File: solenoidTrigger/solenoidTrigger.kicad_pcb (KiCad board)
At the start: 2 copper layers, 88.9 x 88.9 mm, 44 parts, among them J1 Conn_01x09_Female, J8 CONN_02X03, P1 OSTTC03, P2 OSTTC02, P4 OSTTC03, Q1 NMOS_CDS16, Q2 NMOS_CDS16, Q4 NMOS_CDS16, Q5 NMOS_CDS16, U1 L78M05CDT-TR, U2 ATmega328P-AU, Y2 Crystal_SMD

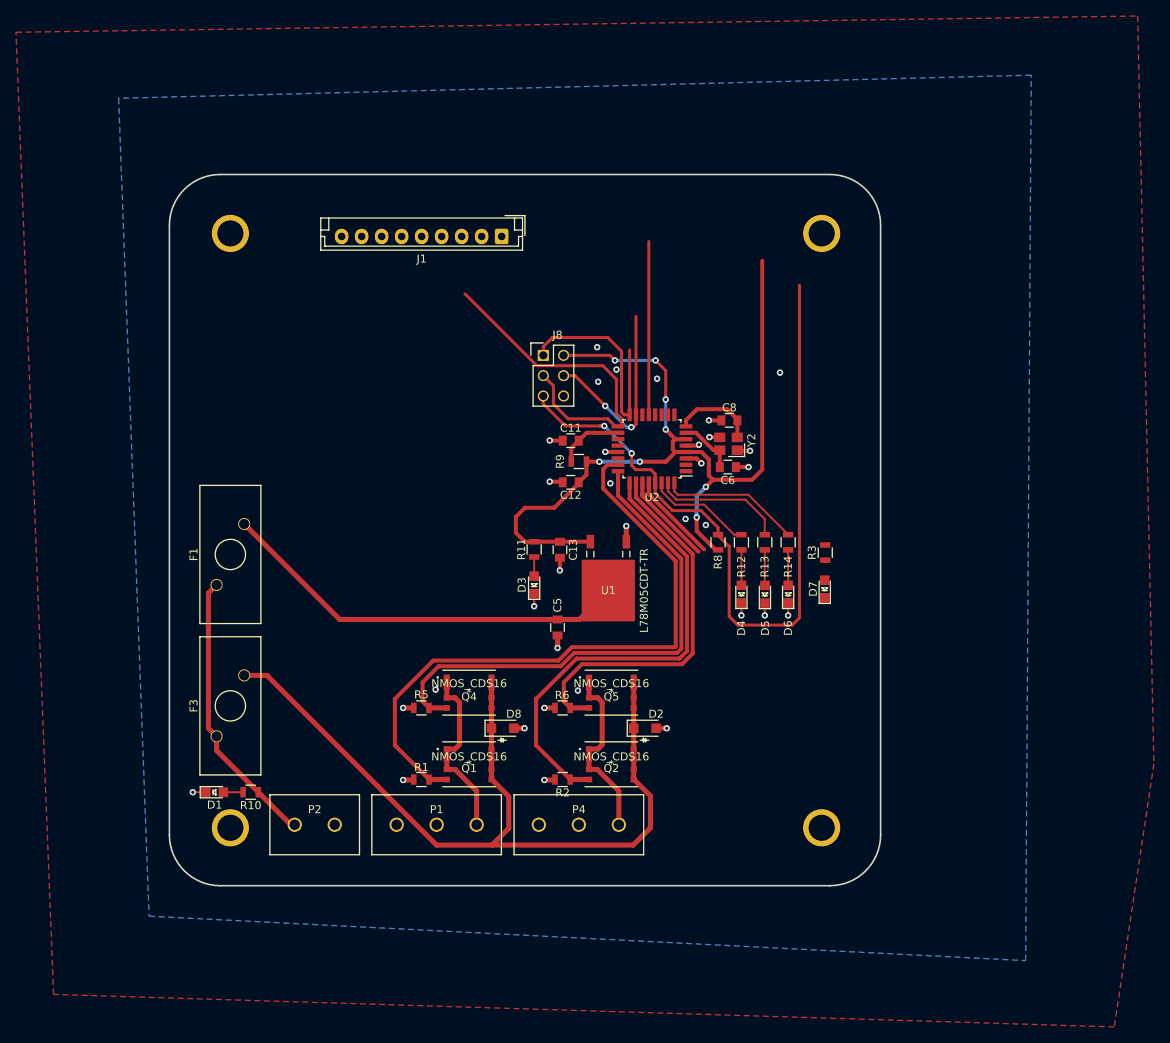
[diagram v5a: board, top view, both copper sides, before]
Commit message: moved components away from mounting holes
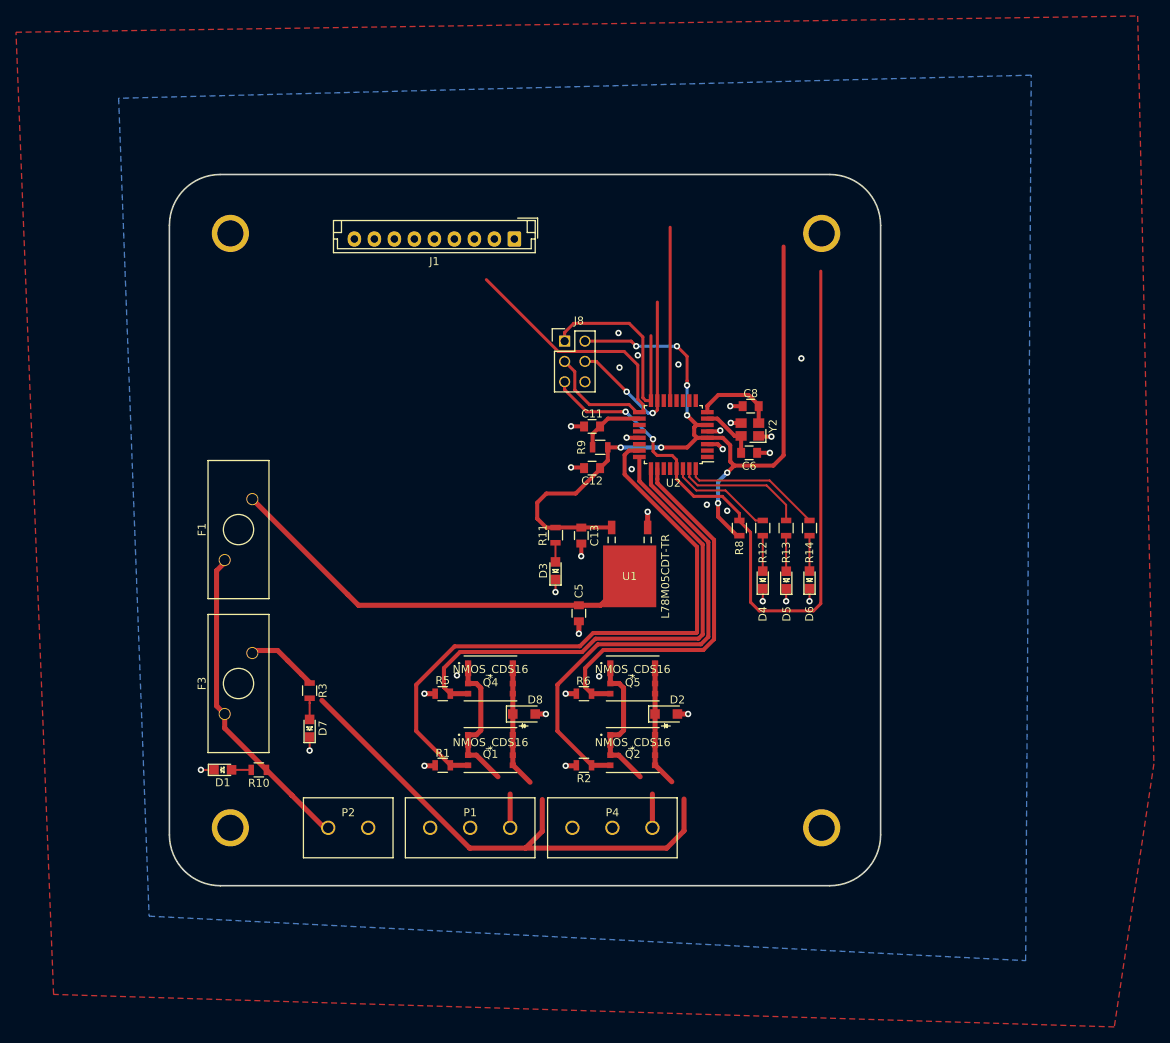
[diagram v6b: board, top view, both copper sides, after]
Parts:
- moved R3 66.7 mm to (120.4, 114.0), turned to 270 degrees
- moved D7 66.7 mm to (120.4, 118.7)
- moved P1 4.21 mm to (140.5, 131.2)
- moved P4 4.21 mm to (158.2, 131.2)
- moved P2 4.21 mm to (125.2, 131.2)
- moved F1 3.27 mm to (111.5, 82.7)
- moved C11 3.21 mm to (155.7, 81.0)
- moved C13 3.21 mm to (154.4, 94.7)
- moved C5 3.21 mm to (154.1, 104.4)
- moved C6 3.21 mm to (175.3, 84.3)
- moved D2 3.21 mm to (165.0, 117.0)
- moved D8 3.21 mm to (147.2, 117.0)
- moved Q1 3.21 mm to (143.0, 121.5)
- moved Q2 3.21 mm to (160.8, 121.5)
- moved R1 3.21 mm to (137.0, 123.4)
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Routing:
- net Net-(D7-Pad2): track 0.00 -> 67.4 mm
- net /12V_Switch: track 103.2 -> 40.5 mm
- net Net-(U2-Pad27): track 11.5 -> 0.00 mm
- net Net-(U2-Pad28): track 11.2 -> 0.00 mm
- net /Source(12V): track 35.1 -> 39.6 mm
- net /12V_Low: track 52.0 -> 54.2 mm
- net GND: track 35.9 -> 37.5 mm, vias 33 -> 34

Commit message: labeling
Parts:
- removed D2, D8: SS110LW, footprints:D_SOD-123W_OEM
- added fly-sol1: SS110LW, footprints:D_SOD-123W_OEM, F.Cu at (140.4, 117.0)
- added fly-sol2: SS110LW, footprints:D_SOD-123W_OEM, F.Cu at (158.2, 117.0)
- moved HFuseLED1 0.64 mm to (120.3, 119.4)
- moved R3 0.64 mm to (120.3, 114.7)
- moved radio_conn1 0.32 mm to (145.9, 57.3)
- renumbered D7 to HFuseLED1, D4 to PLED-1, D5 to PLED-2, D6 to PLED-3, D1 to PowerLED1, D3 to VCCLED1, P2 to battery_conn1, F3 to high_fuse1, U1 to lin_reg1, F1 to low_fuse1, J8 to prog_conn1, R1 to r_tres1_sol1, R2 to r_tres1_sol2, R5 to r_tres2_sol1, R6 to r_tres2_sol2, J1 to radio_conn1, P1 to sol_conn-1, P4 to sol_conn-2, Q1 to tres1_sol1, Q2 to tres1_sol2, Q4 to tres2_sol1, Q5 to tres2_sol2
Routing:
- net /12V_Switch: track 40.5 -> 113.3 mm
- net Net-(HFuseLED1-Pad2): track 67.4 -> 2.65 mm
- net /12V_Solenoid2: track 23.1 -> 25.9 mm
- net /12V_Solenoid1: track 23.1 -> 25.9 mm

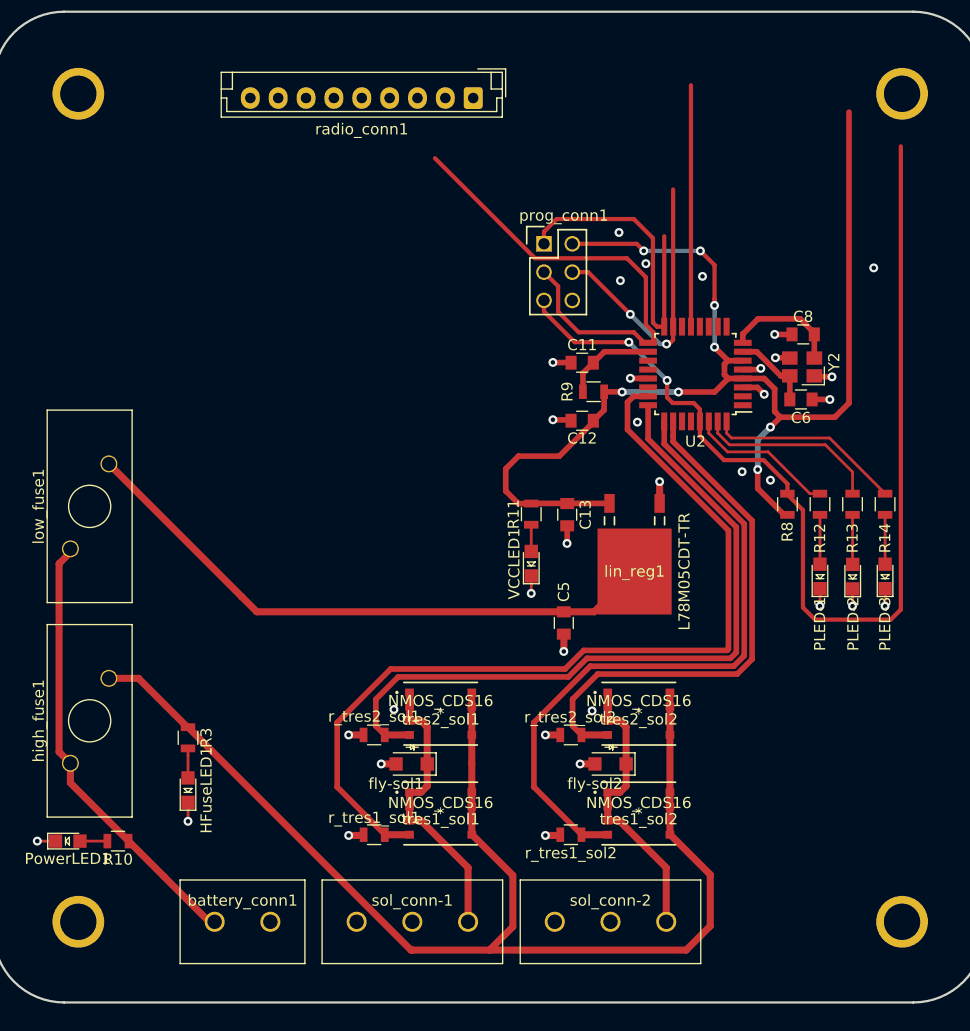
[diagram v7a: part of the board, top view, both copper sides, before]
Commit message: added back 3rd solenoid
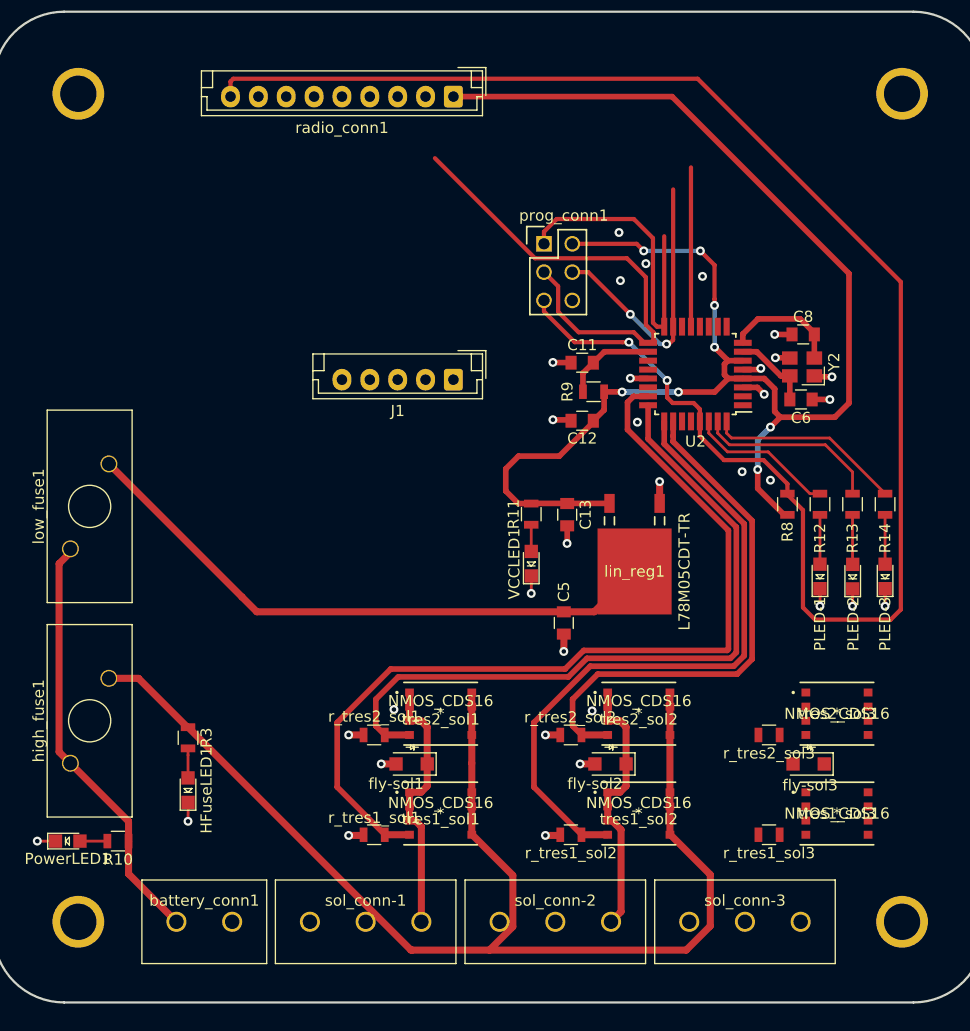
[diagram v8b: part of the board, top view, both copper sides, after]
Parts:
- added J1: Conn_01x05_Female, Connector_JST:JST_EH_B5B-EH-A_1x05_P2.50mm_Vertical, F.Cu at (144.1, 82.5)
- added fly-sol3: SS110LW, footprints:D_SOD-123W_OEM, F.Cu at (176.0, 117.0)
- added r_tres1_sol3: R_1K, footprints:R_0805_OEM, F.Cu at (172.5, 123.4)
- added r_tres2_sol3: R_1K, footprints:R_0805_OEM, F.Cu at (172.5, 114.4)
- added sol_conn-3: OSTTC03, footprints:OSTTC030162, F.Cu at (170.3, 131.2)
- added tres1_sol3: NMOS_CDS16, footprints:CSD16322Q5, F.Cu at (178.6, 121.5)
- added tres2_sol3: NMOS_CDS16, footprints:CSD16322Q5, F.Cu at (178.6, 112.5)
- moved sol_conn-2 4.95 mm to (153.3, 131.2)
- moved sol_conn-1 4.19 mm to (136.3, 131.2)
- moved battery_conn1 3.43 mm to (121.8, 131.2)
- moved radio_conn1 1.78 mm to (144.1, 57.1)
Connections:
- U2 pad 27: Net-(U2-Pad27) -> /ctrl_pin_3-1
- U2 pad 28: Net-(U2-Pad28) -> /ctrl_pin_3-2
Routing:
- net /RESET: track 94.4 -> 151.4 mm
- net VCC: track 112.9 -> 140.5 mm
- net /G0(IRQ): track 21.7 -> 14.3 mm
- net /12V_Solenoid1: track 25.9 -> 23.8 mm
- net /Source(12V): track 39.6 -> 37.9 mm
- net /12V_Solenoid2: track 25.9 -> 24.2 mm
- net GND: vias 34 -> 33
